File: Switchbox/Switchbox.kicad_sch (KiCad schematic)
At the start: 33 parts, among them J1 USB-C_connector, SW1 SW_SPDT, SW2 SW_SPDT, SW3 SW_SPDT, SW4 SW_SPDT, SW5 SW_SPST_LED, SW6 SW_SPDT_BOX, U2 AP63203WU

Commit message: Add buck symbol
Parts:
- added U1: AP63203WU-7, AP63203WU-7_DIO, symbol buck:AP63203WU-7
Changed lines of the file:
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@@
+	)
+	(symbol
+		(lib_id "buck:AP63203WU-7")
+		(at 161.29 21.59 0)
+		(unit 1)
+		(exclude_from_sim no)
+		(in_bom yes)
+		(on_board yes)
+		(dnp no)
+		(fields_autoplaced yes)
+		(property "Reference" "U1"
+			(at 181.61 11.43 0)
+			(effects
+				(font
+					(size 1.524 1.524)
+				)
+			)
+		)
+		(property "Value" "AP63203WU-7"
+			(at 181.61 13.97 0)
+			(effects
+				(font
+					(size 1.524 1.524)
+				)
+			)
+		)
+		(property "Footprint" "AP63203WU-7_DIO"
+			(at 161.29 21.59 0)
+			(effects
+				(font
+					(size 1.27 1.27)
+					(italic yes)
+				)
+				(hide yes)
+			)
+		)
+		(property "Datasheet" "AP63203WU-7"
+			(at 161.29 21.59 0)
+			(effects
+				(font
+					(size 1.27 1.27)
+					(italic yes)
+				)
+				(hide yes)
+			)
+		)
+		(property "Description" ""
+			(at 161.29 21.59 0)
+			(effects
+				(font
+					(size 1.27 1.27)
+				)
+				(hide yes)
+			)
+		)
+		(pin "1"
+		)
+		(pin "2"
+		)
+		(pin "3"
+		)
+		(pin "6"
+		)
+		(pin "5"
+		)
+		(pin "4"
+		)
+		(instances
+			(project ""
+				(path "/d487e400-6779-4fdb-b98e-a608f0bb7bbf"
+					(reference "U1")
+					(unit 1)
+				)
+			)
+		)
 	)
 	(symbol

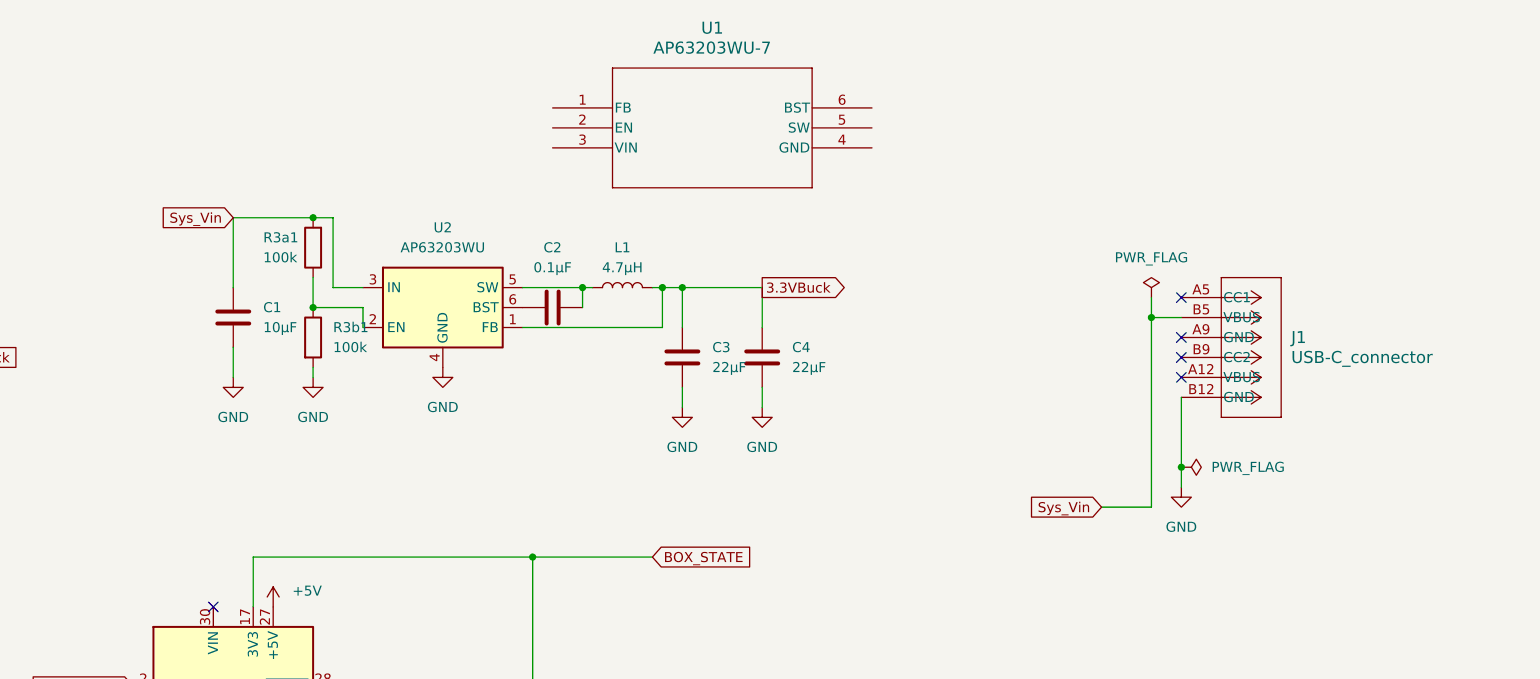
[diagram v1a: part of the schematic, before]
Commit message: Fix buck and USB connector in schematic
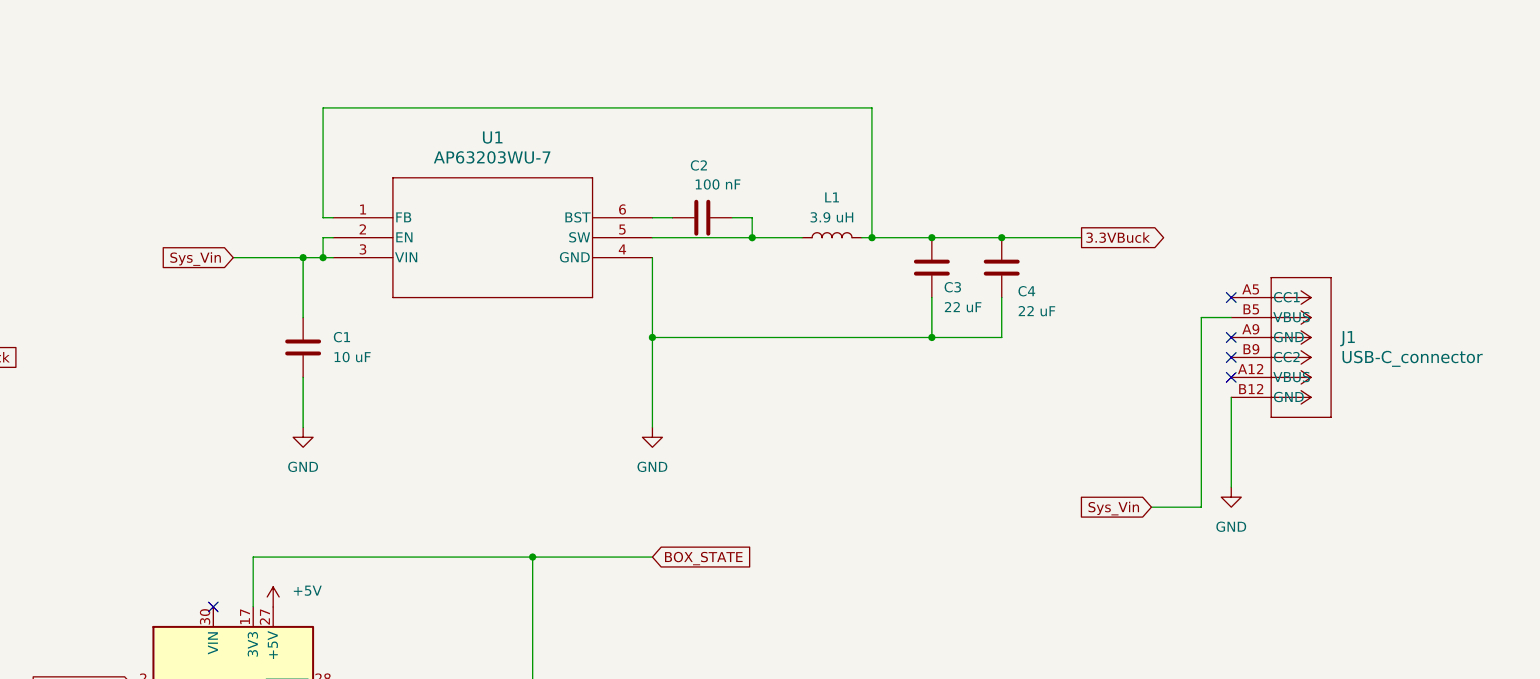
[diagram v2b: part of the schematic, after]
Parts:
- removed R3a1, R3b1: 100k, Resistor_SMD:R_0805_2012Metric_Pad1.20x1.40mm_HandSolder, symbol Device:R
- removed U2: AP63203WU, Package_TO_SOT_SMD:TSOT-23-6, symbol Regulator_Switching:AP63203WU
- C1: value 10µF -> 10 uF
- C2: value 0.1µF -> 100 nF; footprint switchbox_footprints:CAPC0603X33N -> (none)
- C3, C4: value 22µF -> 22 uF
- J1: footprint switchbox_footprints:CONN_484050003_MOL -> switchbox_footprints:CONN_10164359-00011LF_AMP; symbol killswitch:USB-C connector -> usbc-connector:10164359-00011LF
- L1: value 4.7µH -> 3.9 uH
- U1: footprint AP63203WU-7_DIO -> switchbox_footprints:buck
- XBEE1: symbol VectorNav2:Xbee_pro_s3b -> xbee:Xbee_pro_s3b; now in the parts list
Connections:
- net 3.3VBuck: now also U1.1 (FB)
- net GND: now also U1.4 (GND)
- net Sys_Vin: now also U1.2 (EN), U1.3 (VIN)
- net at C2.2, L1.1: now also U1.5 (SW)
- net at U1.6 (BST): now also C2.1
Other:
- moved on the sheet: J1, U1

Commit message: Add missing cap footprint
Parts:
- C2: footprint (none) -> Capacitor_SMD:C_1210_3225Metric_Pad1.33x2.70mm_HandSolder
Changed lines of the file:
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@@
 			)
 		)
-		(property "Footprint" ""
+		(property "Footprint" "Capacitor_SMD:C_1210_3225Metric_Pad1.33x2.70mm_HandSolder"
 			(at 184.15 34.5948 0)
 			(effects

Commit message: Change USB signals, inductor footprint, add voltage divider between Xbee and Nano, route new components, increase trace widths
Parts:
- added R10: 20k, Resistor_SMD:R_0805_2012Metric_Pad1.20x1.40mm_HandSolder, symbol Device:R
- added R11: 10k, Resistor_SMD:R_0805_2012Metric_Pad1.20x1.40mm_HandSolder, symbol Device:R
- added R8, R9: 5.1k, Resistor_SMD:R_0805_2012Metric_Pad1.20x1.40mm_HandSolder, symbol Device:R
- C2: footprint Capacitor_SMD:C_1210_3225Metric_Pad1.33x2.70mm_HandSolder -> Capacitor_SMD:C_0603_1608Metric_Pad1.08x0.95mm_HandSolder
- L1: footprint Inductor_SMD:L_0201_0603Metric_Pad0.64x0.40mm_HandSolder -> switchbox_footprints:IND_BOURNS_SRR5018
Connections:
- net GND: now also J1.A12 (GND), R10.2, R8.1, R9.1
- net Sys_Vin: now also J1.A9 (VBUS), J1.B9 (VBUS); no longer J1.B5 (VBUS)
- net TO_XBEE: now also R11.1; no longer XBEE1.3 (DIN/CONFIG)
- net at J1.A5 (CC1): now also R8.2
- new net: J1.B5 (CC2), R9.2
- new net: R10.1, R11.2, XBEE1.3 (DIN/CONFIG)
- no-connect marks 33 -> 29

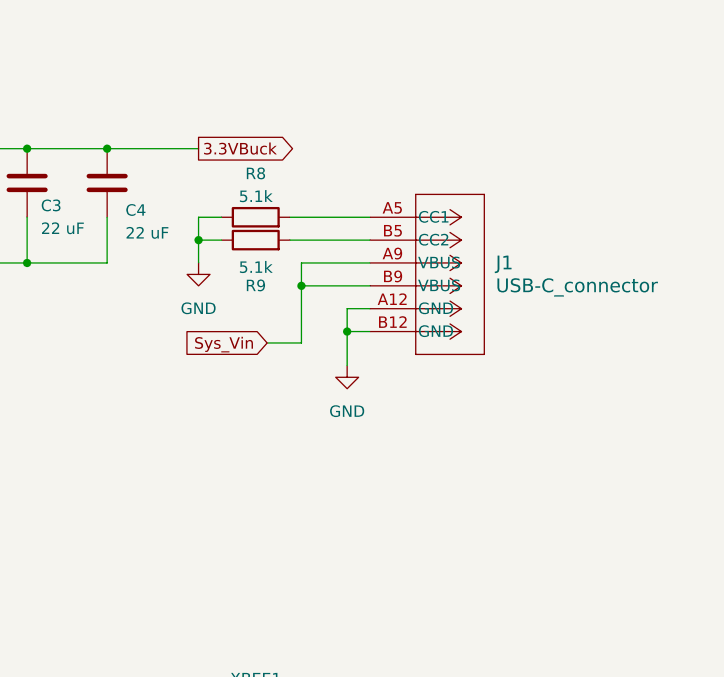
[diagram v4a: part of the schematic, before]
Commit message: add usb-a
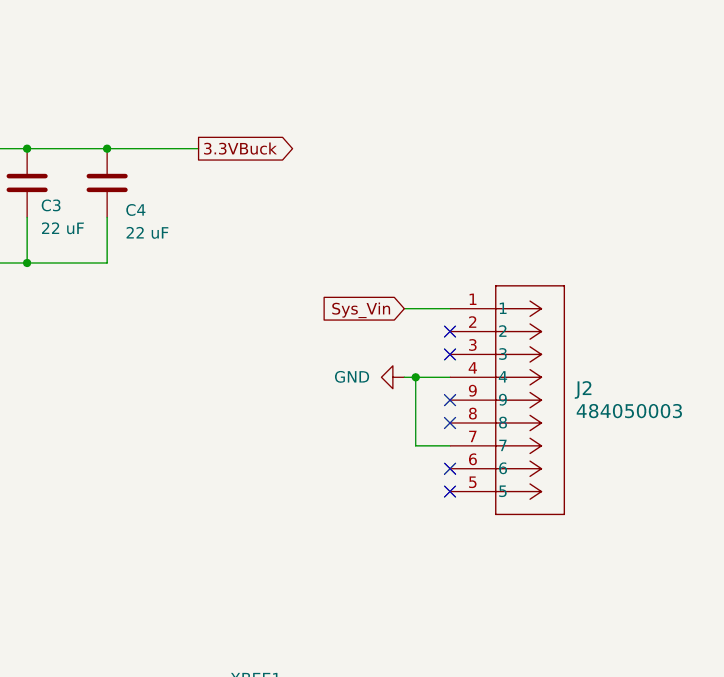
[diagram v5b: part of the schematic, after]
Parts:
- removed J1: USB-C_connector, switchbox_footprints:CONN_10164359-00011LF_AMP, symbol usbc-connector:10164359-00011LF
- removed R8, R9: 5.1k, Resistor_SMD:R_0805_2012Metric_Pad1.20x1.40mm_HandSolder, symbol Device:R
- added J2: 484050003, switchbox_footprints:usba_footprint, symbol usba:484050003
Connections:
- net GND: now also J2.4, J2.7
- net Sys_Vin: now also J2.1
- no-connect marks 29 -> 35
